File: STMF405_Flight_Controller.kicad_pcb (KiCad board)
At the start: 4 copper layers, 40 x 40 mm, 210 parts, among them J1 10155435-00011LF, U1 STM32F405RGTx, U10 ESDS304DBVR, U11 ESD351DPYR, U12 TJA1051TK-3, U13 ATtiny85-20S, U2 AT7456E, U3 TXU0304PWR, U4 ICM-42688-P, U5 MT29F2G01ABAGDWB-IT_G, U6 DPS310XTSA1, U7 AP63205WU, U8 AP63203WU, U9 ESDS304DBVR, Y1 8MHz, Y2 27MHz

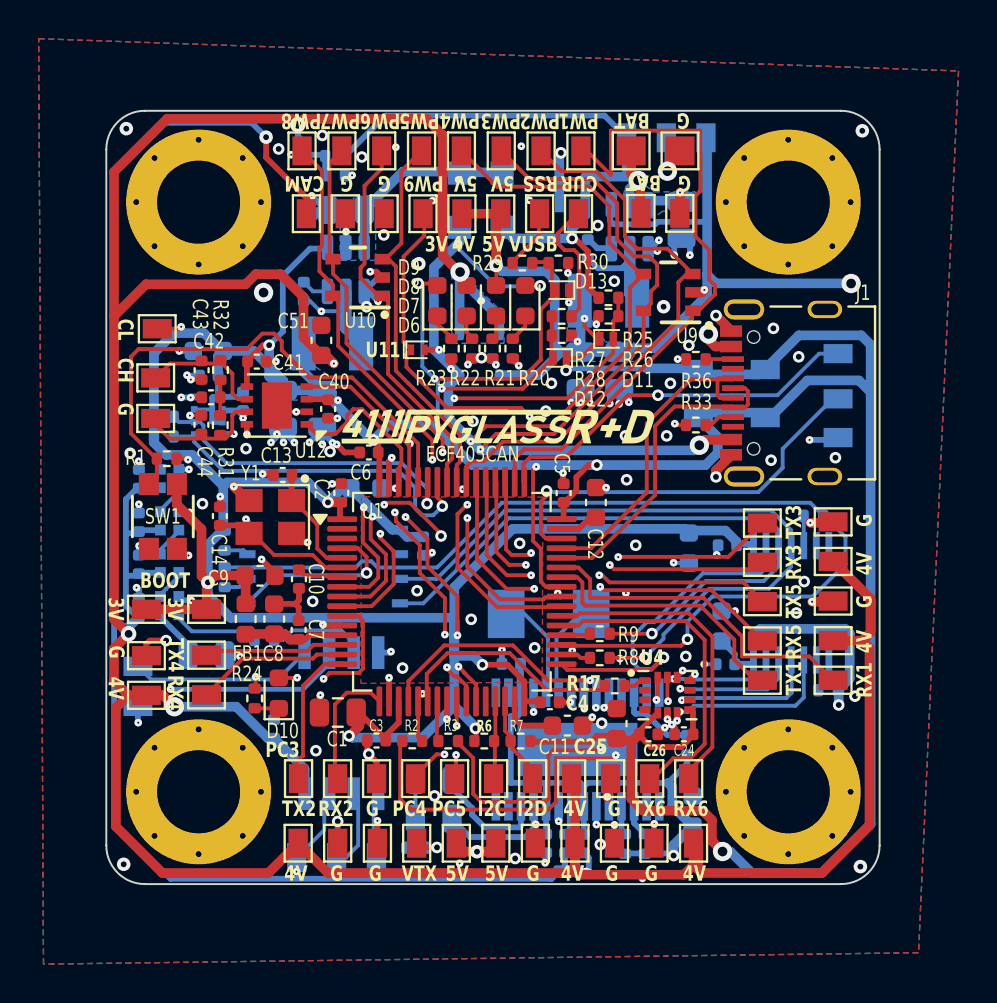
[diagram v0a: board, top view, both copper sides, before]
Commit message: replace flash memory with SD flash memory; move SPI2 terminations closer to source
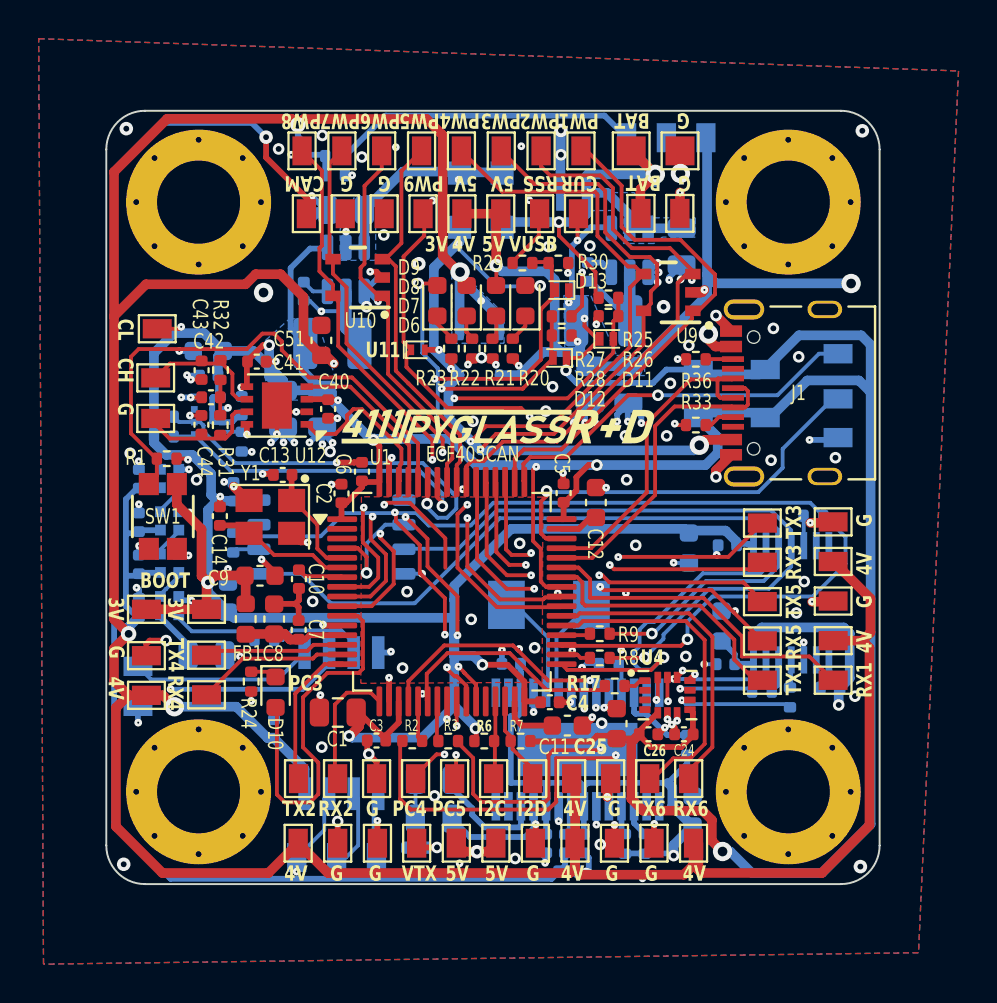
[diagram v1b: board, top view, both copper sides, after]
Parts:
- removed R18: 5k1, Resistor_SMD:R_0402_1005Metric
- added R34: 100k, Resistor_SMD:R_0402_1005Metric, B.Cu at (156.8, 67.4)
- added R35: 22, Resistor_SMD:R_0402_1005Metric, B.Cu at (183.7, 80.3)
- added R40: 22, Resistor_SMD:R_0402_1005Metric, B.Cu at (185.2, 80.6)
- added R41: 22, Resistor_SMD:R_0402_1005Metric, B.Cu at (175.8, 78.9)
- L1, L2: footprint Project:IND_DFE322520FD-4R7M=P2_MUR -> Inductor_SMD:L_1210_3225Metric
- R20, R21: value 3k3 -> 1k5
- R22: value 3k3 -> 1k2
- R23, R24: value 1k2 -> 680
- SW1: value ~ -> EVP-AA602W
- U5: value MT29F2G01ABAGDWB-IT_G -> XTSD04G; footprint Project:SON127P600X800X65-8N -> Package_LGA:LGA-8_8x6mm_P1.27mm
- moved C27 10.2 mm to (156.4, 70.0), turned to 90 degrees
- moved C28 9.08 mm to (156.1, 75.4), turned to 90 degrees
- moved R19 1.84 mm to (156.4, 72.6)
- moved U5 1.58 mm to (161.5, 72.3), turned to 180 degrees
- moved C33 1.38 mm to (179.6, 57.3)
- moved U7 1.22 mm to (176.9, 57.5)
- moved C32 1.19 mm to (174.7, 58.6)
- moved L1 1.07 mm to (175.5, 61.1)
- moved C6 1.05 mm to (163.1, 68.9), turned to 90 degrees
- moved C34 0.89 mm to (174.9, 64.4)
- moved R24 0.89 mm to (157.3, 79.8), turned to 90 degrees
- moved C35 0.89 mm to (176.8, 64.5)
- moved G*** 0.86 mm to (173.0, 70.3)
- moved Y2 0.47 mm to (172.7, 75.8)
- moved C29 0.24 mm to (156.8, 65.5), turned to 90 degrees
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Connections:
- R19 pad 1: Net-(U5-SO/IO1) -> Net-(U5-SD0/DO)
- U2 pad 11: /Peripherals/SPI2_MISO_4V -> Net-(U2-SDOUT)
- U3 pad 11: /Peripherals/SPI2_SCK_4V -> Net-(U3-B3Y)
- U3 pad 12: /Peripherals/SPI2_MOSI_4V -> Net-(U3-B2Y)
- U5 pad 1: SPI2_CS_FLASH -> unconnected-(U5-SD2-Pad1)
- U5 pad 2: Net-(U5-SO/IO1) -> SPI2_CS_FLASH
- U5 pad 3: Net-(U5-WP/IO2) -> SPI2_SCK
- U5 pad 5: +3V3 -> SPI2_MOSI
- U5 pad 6: unconnected-(U5-HOLD/IO3-Pad6) -> Net-(U5-SD0/DO)
- U5 pad 7: SPI2_SCK -> unconnected-(U5-SD1-Pad7)
- U5 pad 8: SPI2_MOSI -> +3V3
- U6 pad 2: +3V3 -> unconnected-(U6-~{CSB}-Pad2)_1
- U6 pad 5: GND -> Net-(U6-SDO)
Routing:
- net LED: track 8.25 -> 19.7 mm, vias 2 -> 0
- net +3V3: track 264.7 -> 255.8 mm, vias 13 -> 12
- net SPI2_MOSI: track 34.1 -> 41.6 mm
- net GND: track 112.3 -> 119.8 mm, vias 183 -> 185
- net TIM2_CH1_PWM1: track 33.5 -> 27.4 mm
- net +BATT: track 40.7 -> 44.3 mm
- net I2C1_SDA: track 17.0 -> 20.4 mm
- net SPI2_CS_FLASH: track 9.09 -> 6.33 mm
- net /Peripherals/SPI2_MOSI_4V: track 11.9 -> 9.47 mm
- net Net-(U2-SDOUT): track 0.00 -> 2.35 mm
- net /Peripherals/SPI2_MISO_4V: track 12.6 -> 14.9 mm
- net +5V: track 150.5 -> 152.6 mm
- net /Peripherals/SPI2_SCK_4V: track 12.2 -> 10.6 mm
- net Net-(U3-B2Y): track 0.00 -> 1.55 mm
- net Net-(U3-B3Y): track 0.00 -> 1.46 mm
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
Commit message: relabel components by sheet and block
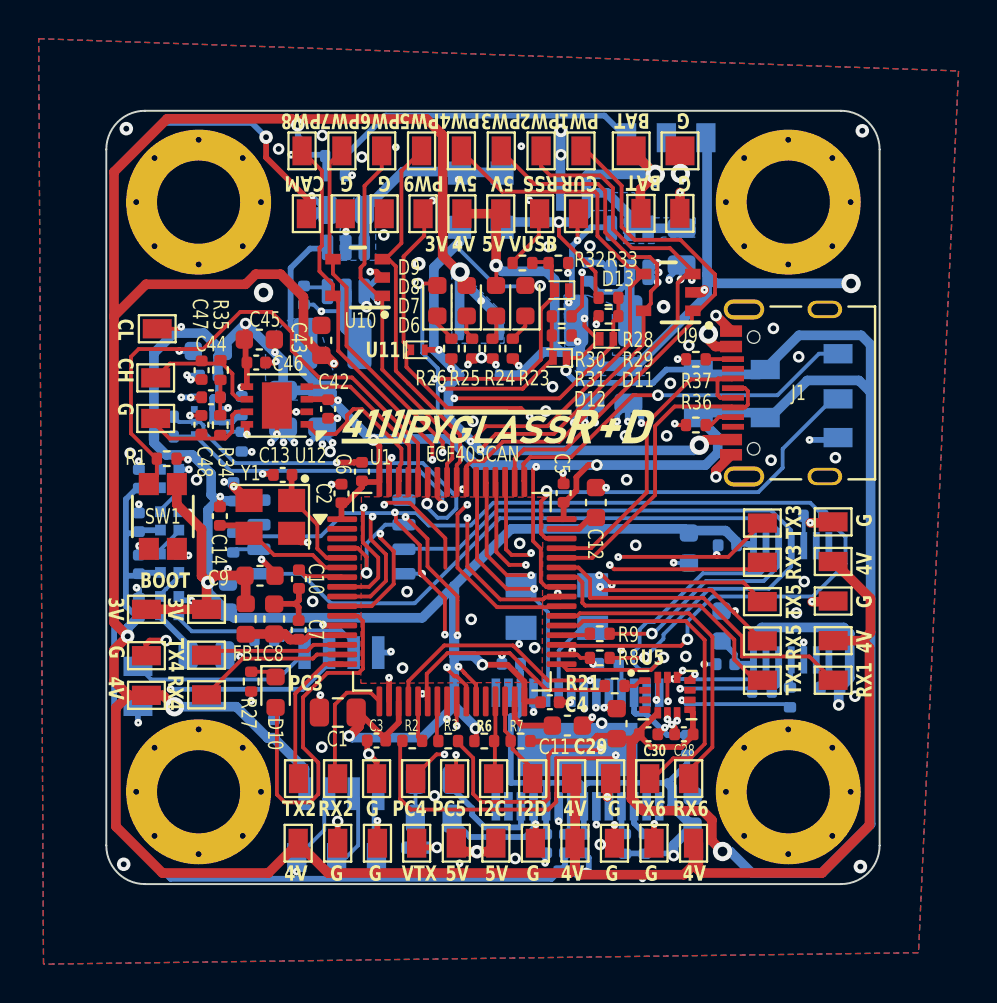
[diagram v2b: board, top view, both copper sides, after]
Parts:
- added C45: 2u2, Capacitor_SMD:C_0603_1608Metric, F.Cu at (157.7, 62.1)
- R40: renamed from R39; value 560 -> 680
- Y2: footprint Crystal:Crystal_SMD_0603-2Pin_6.0x3.5mm -> Project:XTAL_ECS-270-20-30B-TR
- moved Y2 0.42 mm to (173.1, 75.9)
- moved C38 0.20 mm to (160.1, 59.8)
- moved C46 0.06 mm to (157.6, 63.3)
- renumbered C27 to C22, C28 to C23, C53 to C24, C22 to C25, C23 to C26, C52 to C27, C24 to C28, C25 to C29, C26 to C30, C29 to C31, C30 to C32, C31 to C33, C32 to C34, C33 to C35, C34 to C36, C35 to C37, C36 to C38, C37 to C39, C38 to C40, C39 to C41, C40 to C42, C51 to C43, C42 to C44, C41 to C46, C43 to C47, C44 to C48, C45 to C49, C48 to C50, C49 to C51, C46 to C52, C47 to C53, C50 to C54, D4 to D3, D3 to D4, R41 to R12, R12 to R13, R13 to R14, R14 to R15, R19 to R16, R35 to R17, R40 to R18, R15 to R19, R16 to R20, R17 to R21, R34 to R22, R20 to R23, R21 to R24, R22 to R25, R23 to R26, R24 to R27, R25 to R28, R26 to R29, R27 to R30, R28 to R31, R29 to R32, R30 to R33, R31 to R34, R32 to R35, R33 to R36, R36 to R37, R37 to R38, R38 to R39, TP68 to TP25, TP69 to TP26, TP70 to TP27, TP71 to TP28, TP25 to TP29, TP37 to TP30, TP26 to TP31, TP38 to TP32, TP27 to TP33, TP39 to TP34, TP28 to TP35, TP40 to TP36, TP29 to TP37, TP41 to TP38, TP30 to TP39, TP42 to TP40, TP31 to TP41, TP43 to TP42, TP32 to TP43, TP33 to TP45, TP45 to TP46, TP34 to TP47, TP46 to TP48, TP35 to TP49, TP47 to TP50, TP36 to TP51, TP48 to TP52, TP65 to TP53, TP66 to TP54, TP67 to TP55, TP75 to TP56, TP76 to TP57, TP49 to TP58, TP50 to TP59, TP51 to TP60, TP52 to TP61, TP53 to TP62, TP54 to TP63, TP55 to TP64, TP56 to TP65, TP57 to TP66, TP58 to TP67, TP59 to TP68, TP60 to TP69, TP61 to TP70, TP62 to TP71, TP63 to TP72, TP64 to TP73, TP72 to TP74, TP73 to TP75, TP74 to TP76, U5 to U3, U3 to U4, U4 to U5
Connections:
- net Net-(U2-XFB) renamed /Peripherals/XFB
- U2 pad 5: Net-(U2-CLKIN) -> /Peripherals/CLKIN
- Y2 pad 2: Net-(U2-CLKIN) -> GND
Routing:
- net /Peripherals/CLKIN: track 0.00 -> 6.35 mm
- net Net-(U2-CLKIN): track 6.08 -> 0.00 mm
- net +3V3: track 255.8 -> 258.0 mm
- net GND: track 119.8 -> 121.8 mm, vias 185 -> 186
- net /Peripherals/XFB: track 6.10 -> 4.67 mm
- net Net-(U1-BOOT0): track 27.3 -> 28.5 mm
- net /Peripherals/SPI2_MISO_4V: track 14.9 -> 13.8 mm
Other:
- board text added: "mgi 0724"
- board text removed: "mgi 0424"

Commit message: remove blind vias and use 0201 resistors
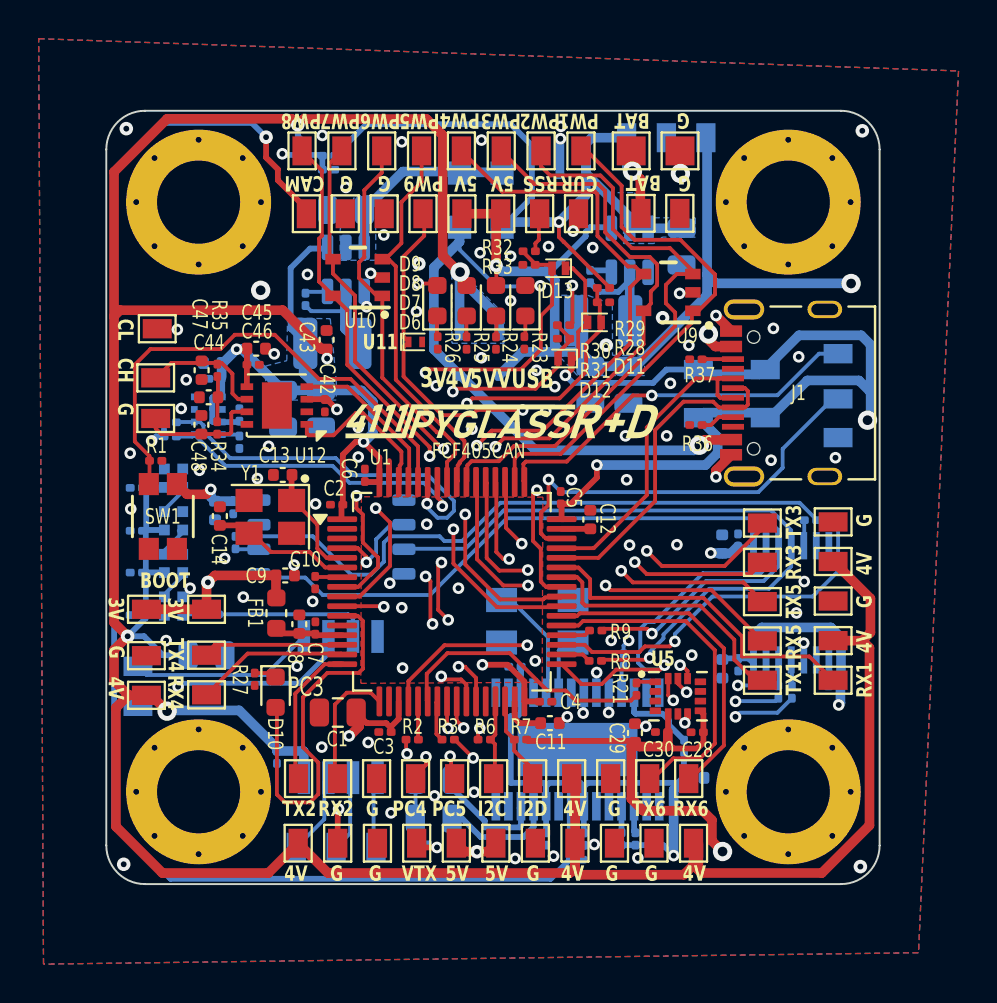
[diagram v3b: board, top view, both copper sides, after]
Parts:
- C10, C18, C19, C2, C20, C21, C22, C25, C26, C28, C3, C30, C31, C33, C34, C38, C4, C42, C46, C49, C5, C51, C52, C53, C54, C6, C7: footprint Capacitor_SMD:C_0402_1005Metric -> Project:C_0201_0603Metric
- C11, C12, C17, C23, C24, C27, C29, C32, C43, C45, C8, C9: footprint Capacitor_SMD:C_0603_1608Metric -> Capacitor_SMD:C_0402_1005Metric
- D10: value YELLOW GPIO -> ORANGE GPIO
- R1, R10, R11, R12, R13, R14, R15, R16, R17, R18, R19, R2, R20, R21, R22, R23, R24, R25, R26, R27, R28, R29, R3, R30, R31, R32, R33, R34, R35, R36, R37, R38, R39, R4, R40, R5, R6, R7, R8, R9: footprint Resistor_SMD:R_0402_1005Metric -> Project:R_0201_0603Metric
- moved C23 4.53 mm to (155.4, 71.0), turned to -90 degrees
- moved R40 3.00 mm to (155.3, 76.3)
- moved C27 2.22 mm to (181.7, 79.1), turned to -90 degrees
- moved C24 1.73 mm to (181.7, 72.7), turned to 90 degrees
- moved C17 1.72 mm to (180.3, 84.8), turned to 0 degrees
- moved D1 1.64 mm to (174.0, 52.9)
- moved FB1 1.61 mm to (158.6, 76.3)
- moved R33 1.52 mm to (171.7, 58.2), turned to 180 degrees
- moved C49 1.47 mm to (158.7, 83.7), turned to -90 degrees
- moved C8 1.33 mm to (159.8, 76.8)
- moved C9 1.31 mm to (159.1, 74.3)
- moved Y2 1.26 mm to (172.1, 76.7)
- moved D13 1.14 mm to (173.2, 58.4)
- moved R21 1.14 mm to (177.2, 80.2), turned to 90 degrees
- moved C29 1.06 mm to (177.2, 82.5)
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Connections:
- net /Pinout with components/CH renamed /Pinout with components/CANH
- net /Pinout with components/CL renamed /Pinout with components/CANL
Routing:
- net GND: track 121.8 -> 20.5 mm, vias 186 -> 88
- net +3V3: track 258.0 -> 249.1 mm, vias 12 -> 14
- net USART3_TX: track 17.7 -> 23.3 mm
- net /Peripherals/SPI2_MOSI_4V: track 9.47 -> 14.5 mm
- net /Peripherals/SPI2_CS_OSI_4V: track 11.9 -> 16.4 mm
- net +4V: track 186.5 -> 182.8 mm
- net Net-(LED1-DIN): track 4.56 -> 1.23 mm
- net TIM8_Ch3_PWM4: track 41.0 -> 44.0 mm
- net /Power Monitor/DOUT: track 5.09 -> 7.96 mm
- net /Peripherals/SPI2_SCK_4V: track 10.6 -> 13.4 mm
- net Net-(U1-BOOT0): track 28.5 -> 26.0 mm
- net VBUS: track 41.3 -> 39.1 mm
- net SPI1_MOSI: track 17.4 -> 15.4 mm
- net SPI1_MISO: track 12.0 -> 13.9 mm
- net Net-(U1-VDDA): track 5.35 -> 3.55 mm
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
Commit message: double check BOM
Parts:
- C8, C9: value 1u -> 2u2
- D4, D5: value PMEG60T30ELRX -> PMEG3030CERX
- R1: value 22k -> 22k1
- R38: value 20k5 -> 22k1
- R39: value 4k99 -> 5k36
- U3: value XTSD04G -> CSNP4GCR01-AMW

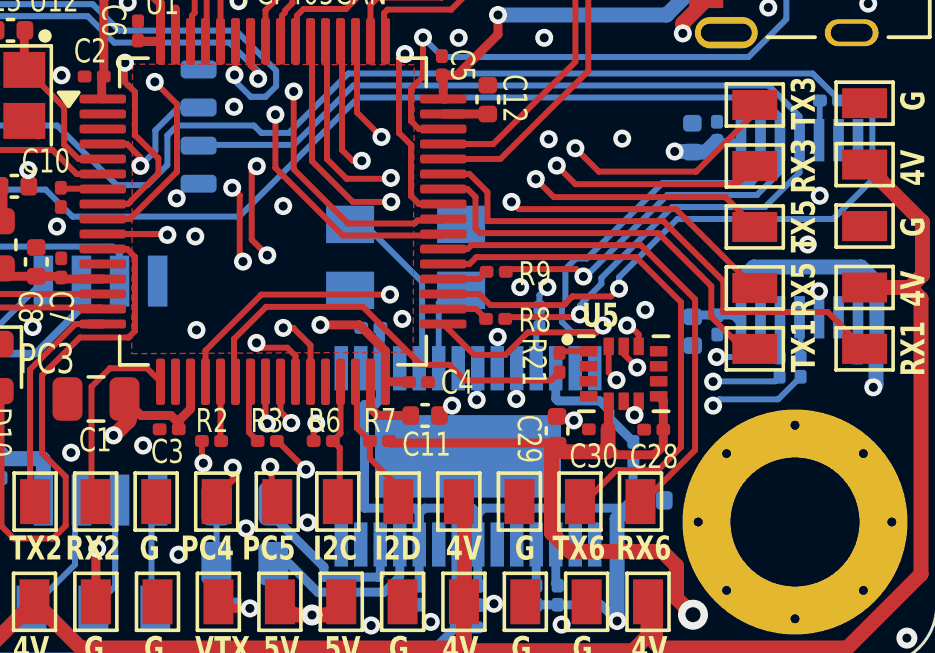
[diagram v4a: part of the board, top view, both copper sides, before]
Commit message: remove soldermask bridges for IMU to faciliate assembly by PCBWAY
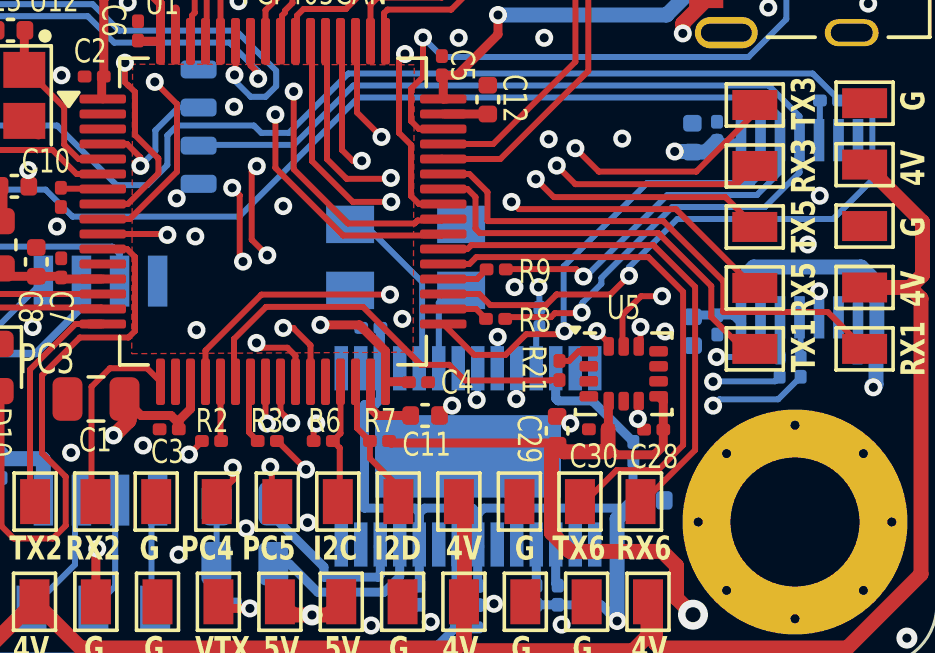
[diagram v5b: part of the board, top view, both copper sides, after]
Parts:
- U5: footprint Project:PQFN50P300X250X97-14N -> Project:LGA-14_3x2.5mm_P0.5mm_LayoutBorder3x4y_no_mask_bridges
- moved R21 0.26 mm to (177.2, 80.5)
- moved R9 0.08 mm to (175.1, 77.1)
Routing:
- net SPI1_SCK: track 20.5 -> 26.4 mm
- net SPI2_CS_OSI: track 18.3 -> 15.7 mm
- net SPI1_CS_IMU: track 18.3 -> 19.4 mm
- net SPI1_MOSI: track 15.4 -> 16.0 mm
